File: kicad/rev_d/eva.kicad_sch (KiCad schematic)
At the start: 0 parts

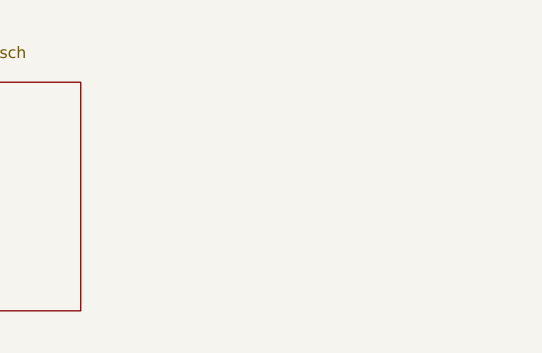
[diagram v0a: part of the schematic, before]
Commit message: pentevo: add VG93 12v switcher (no 12v until voltages on both +5v and +12v busses are OK)
git-svn-id: svn://localhost/local-pentevo@1191 c6c76956-fad2-4150-a3a9-ea0a427205ba
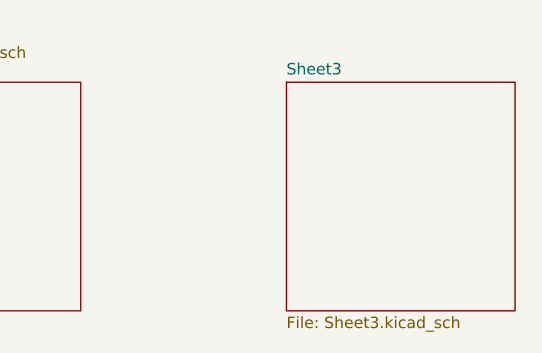
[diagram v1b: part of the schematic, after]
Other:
- added sheet Sheet3 (Sheet3.kicad_sch)
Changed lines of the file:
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@@
+	)
+	(sheet
+		(at 124.46 76.2)
+		(size 25.4 25.4)
+		(fields_autoplaced yes)
+		(stroke
+			(width 0.1524)
+			(type solid)
+		)
+		(fill
+			(color 128 255 128 1.0000)
+		)
+		(property "Sheetname" "Sheet3"
+			(at 124.46 75.4884 0)
+			(effects
+				(font
+					(size 1.27 1.27)
+				)
+				(justify left bottom)
+			)
+		)
+		(property "Sheetfile" "Sheet3.kicad_sch"
+			(at 124.46 102.1846 0)
+			(effects
+				(font
+					(size 1.27 1.27)
+				)
+				(justify left top)
+			)
+		)
+		(instances
+			(project "eva"
+				(path "/ab605654-a730-497b-9e09-9b351f74b935"
+					(page "4")
+				)
+			)
+		)
 	)
 	(sheet

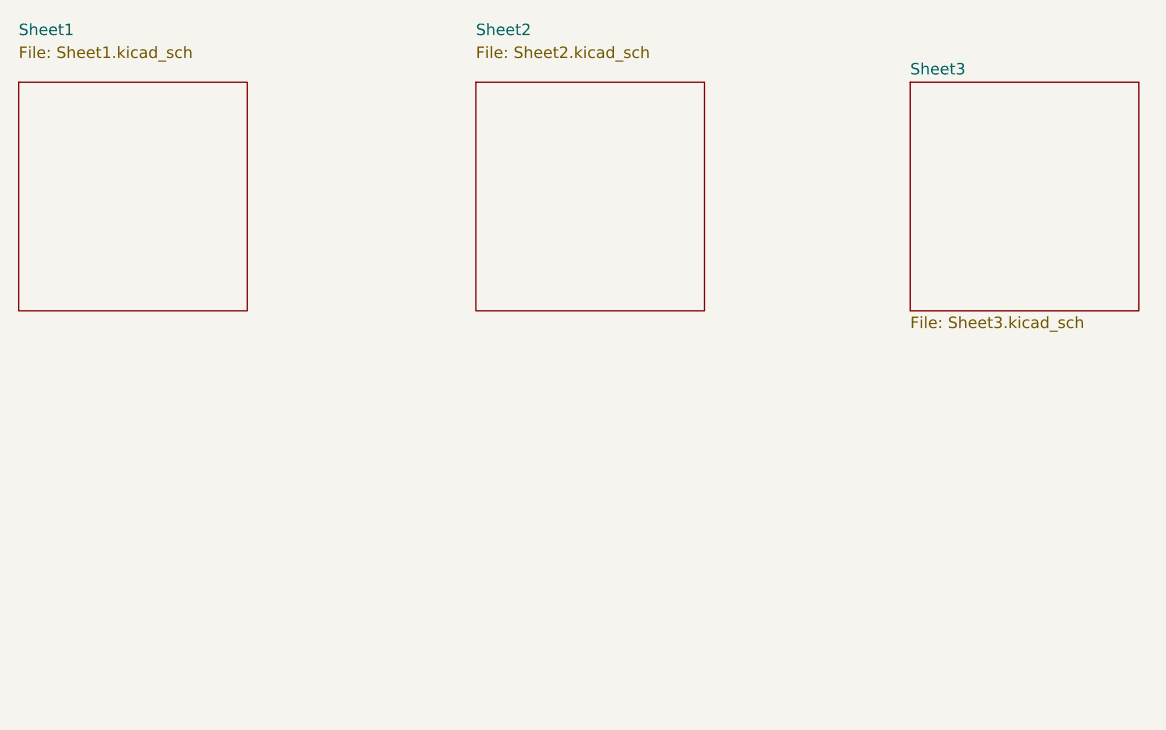
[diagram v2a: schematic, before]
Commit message: pentevo: rev D: video output: make new sheet for video outputs
git-svn-id: svn://localhost/local-pentevo@1274 c6c76956-fad2-4150-a3a9-ea0a427205ba
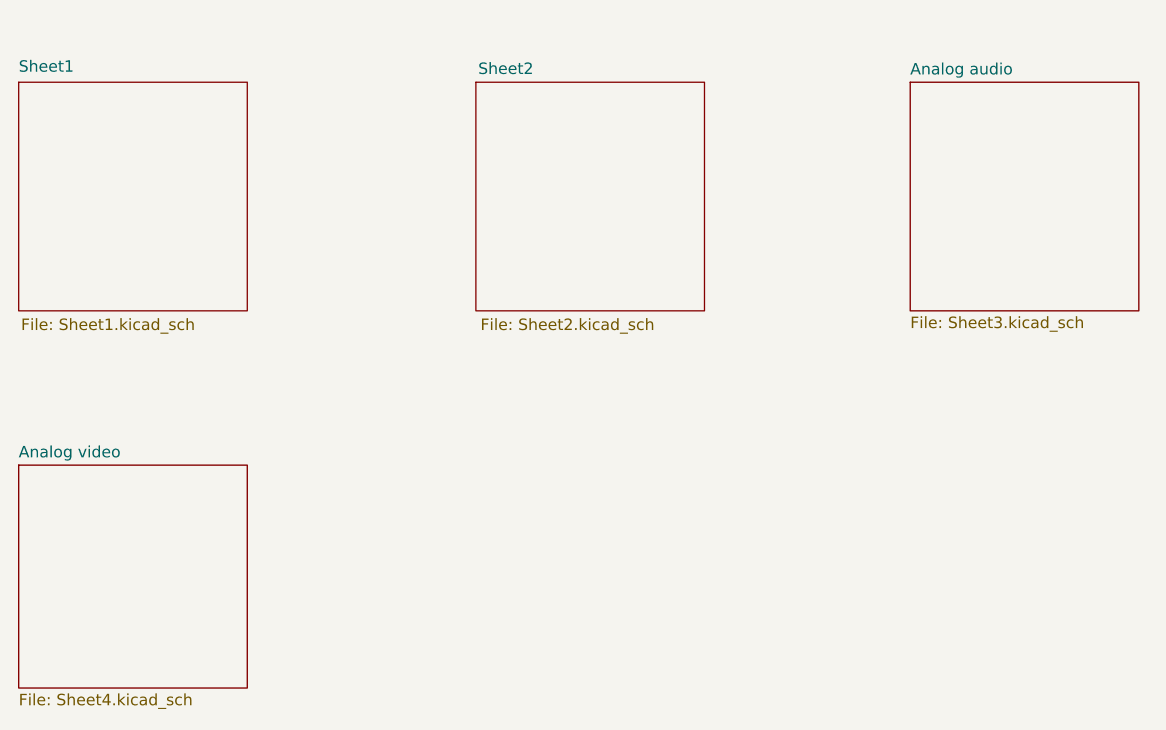
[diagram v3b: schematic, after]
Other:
- sheet Sheet3 renamed Analog audio
- added sheet Analog video (Sheet4.kicad_sch)
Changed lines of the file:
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@@
 	(paper "User" 558.8 431.8)
+	(sheet
+		(at 25.4 118.745)
+		(size 25.4 24.765)
+		(fields_autoplaced yes)
+		(stroke
+			(width 0.1524)
+			(type solid)
+		)
+		(fill
+			(color 137 68 255 1.0000)
+		)
+		(property "Sheetname" "Analog video"
+			(at 25.4 118.0334 0)
+			(effects
+				(font
+					(size 1.27 1.27)
+				)
+				(justify left bottom)
+			)
+		)
+		(property "Sheetfile" "Sheet4.kicad_sch"
+			(at 25.4 144.0946 0)
+			(effects
+				(font
+					(size 1.27 1.27)
+				)
+				(justify left top)
+			)
+		)
+		(instances
+			(project "eva"
+				(path "/ab605654-a730-497b-9e09-9b351f74b935"
+					(page "5")
+				)
+			)
+		)
+	)
 	(sheet
 		(at 76.2 76.2)
 		(size 25.4 25.4)
-		(fields_autoplaced yes)
 		(stroke
 			(width 0)
@@
 		)
 		(property "Sheetname" "Sheet2"
-			(at 76.2 71.12 0)
+			(at 76.454 75.438 0)
 			(effects
 				(font
@@
 		)
 		(property "Sheetfile" "Sheet2.kicad_sch"
-			(at 76.2 73.66 0)
+			(at 76.708 103.886 0)
 			(effects
 				(font
@@
 		)
 		(fill
-			(color 128 255 128 1.0000)
+			(color 255 119 0 1.0000)
 		)
-		(property "Sheetname" "Sheet3"
+		(property "Sheetname" "Analog audio"
 			(at 124.46 75.4884 0)
 			(effects
@@
 		(at 25.4 76.2)
 		(size 25.4 25.4)
-		(fields_autoplaced yes)
 		(stroke
 			(width 0)
@@
 		)
 		(property "Sheetname" "Sheet1"
-			(at 25.4 71.12 0)
+			(at 25.4 75.184 0)
 			(effects
 				(font
@@
 		)
 		(property "Sheetfile" "Sheet1.kicad_sch"
-			(at 25.4 73.66 0)
+			(at 25.654 103.886 0)
 			(effects
 				(font
